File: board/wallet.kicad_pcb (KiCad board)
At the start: 4 copper layers, 48 x 85 mm, 108 parts, among them J1 TYPE-C-31-M-12, U1 BQ25185DLHR, U11 E73-2G4M08S1C, U12 ME6211C28M5G-N, U13 TPS60230RGTR, U14 TLV70313DBVR, U15 MAX17048G+T10, U2 TPS63802DLAR, U4 STM32U585VIT6Q, U5 SE050E2HQ1/Z01Z3Z, U6 TS3USB221ARSER, U7 SN74LVC1G02DBVR(UMW), U8 TPS22917DBVR, U9 TXU0202DCUR

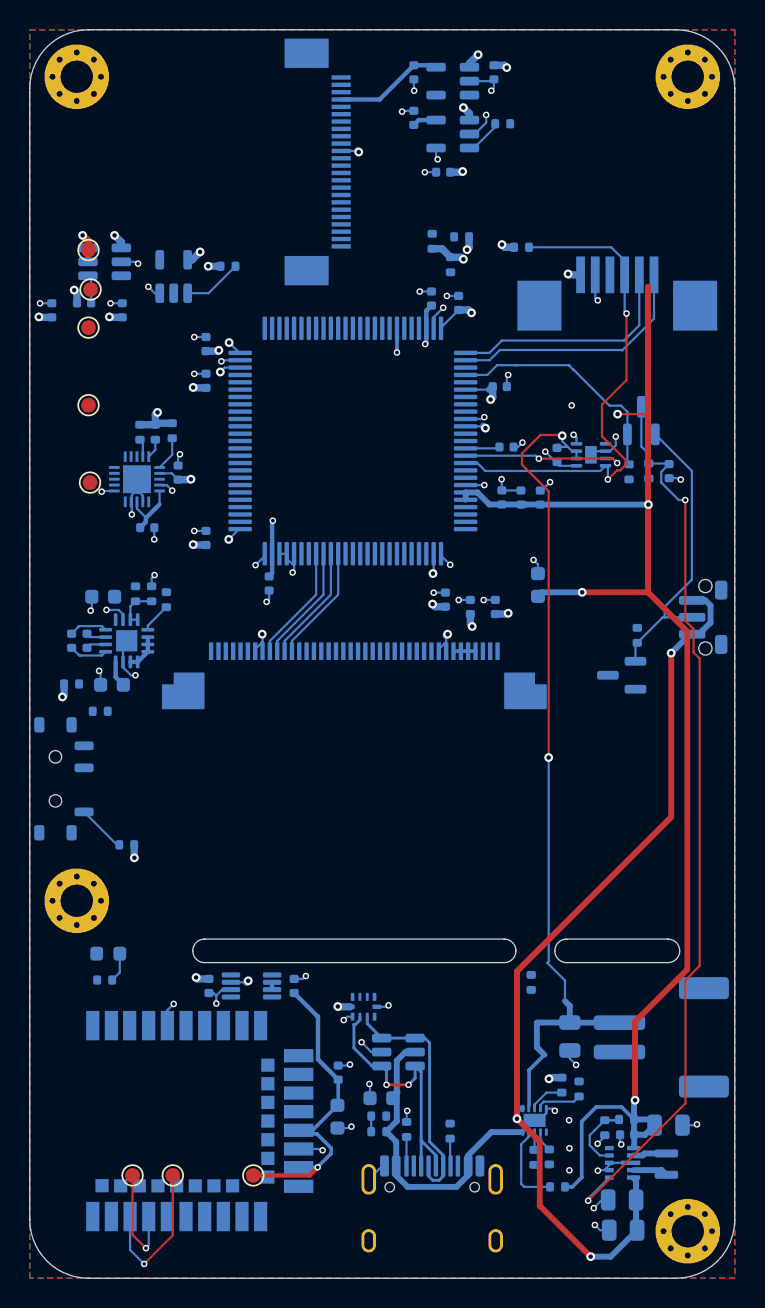
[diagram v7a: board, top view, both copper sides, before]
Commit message: Front copper freed: V3V3 runs made redundant by the In1 plane removed
With In1 a 3.3 V plane every V3V3 pin already has its via, so the owner's
3.3 V runs on the front copper carried nothing but took 64.6 mm of the layer
kept for the buses (incl. the 8.5 mm dangling stub). Removed with KiCad's own
unconnected count as the oracle: flat at 61 (the TP_3V3 front-pad link, which
did depend on it, is kept). The buck-boost's output now enters the plane
through three vias at C_3V3 (two added, each >= 0.25 mm of bare board from
every pad). Also: a 0.02 mm micro-jog on RADIO_3V3 (a 90-degree corner) gone.

Audit (carrier suite run on this board, its ledger and current budget are the
carrier's): of the craft/corner/snaking/width/return-path findings only the
RADIO_3V3 corner and a 2 mm FB_3V3 hop around a GND via were in my copper;
the rest are in the hand-routed chin and east side.

Co-Authored-By: Claude Opus 5.5 <noreply@anthropic.com>
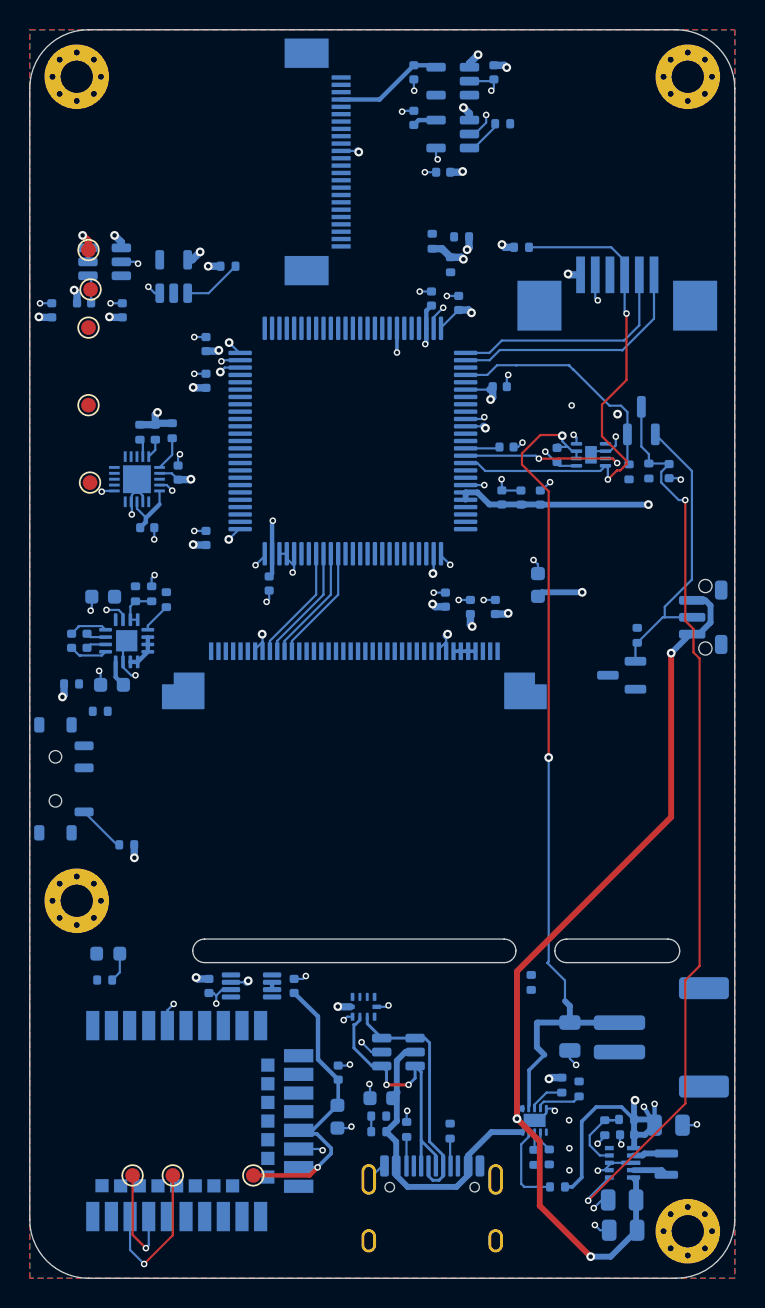
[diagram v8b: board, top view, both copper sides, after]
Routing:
- net V3V3: track 147.0 -> 85.3 mm, vias 43 -> 45
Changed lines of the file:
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@@
-	)
-	(segment
-		(start 42.09 26.01)
-		(end 42.09 17.49)
-		(width 0.4)
-		(layer "F.Cu")
-		(net "V3V3")
-	)
-	(segment
-		(start 42.09 38.3)
-		(end 42.09 26.01)
-		(width 0.4)
-		(layer "F.Cu")
-		(net "V3V3")
-	)
-	(segment
-		(start 37.61 38.3)
-		(end 42.09 38.3)
-		(width 0.4)
-		(layer "F.Cu")
-		(net "V3V3")
-	)
-	(segment
-		(start 44.76459 63.97541)
-		(end 41.21 67.53)
-		(width 0.4)
-		(layer "F.Cu")
-		(net "V3V3")
-	)
-	(segment
-		(start 42.09 38.3)
-		(end 44.76459 40.97459)
-		(width 0.4)
-		(layer "F.Cu")
-		(net "V3V3")
-	)
-	(segment
-		(start 44.76459 40.97459)
-		(end 44.76459 63.97541)
-		(width 0.4)
-		(layer "F.Cu")
-		(net "V3V3")
 	)
 	(segment
@@
 		(net "V3V3")
 	)
-	(segment
-		(start 40.02 26.17)
-		(end 41.93 26.17)
-		(width 0.15)
-		(layer "F.Cu")
-		(net "V3V3")
-	)
-	(segment
-		(start 41.93 26.17)
-		(end 42.09 26.01)
-		(width 0.15)
-		(layer "F.Cu")
-		(net "V3V3")
-	)
-	(segment
-		(start 41.21 67.53)
-		(end 41.21 72.88)
-		(width 0.4)
-		(layer "F.Cu")
-		(net "V3V3")
-	)
 	(via
 		(at 14.875 64.75)
@@
 	)
 	(via
+		(at 42.54 73.13)
+		(size 0.45)
+		(drill 0.25)
+		(layers "F.Cu" "B.Cu")
+		(net "V3V3")
+	)
+	(via
 		(at 10.975 30.6)
 		(size 0.6)
@@
 		(size 0.6)
 		(drill 0.3)
+		(layers "F.Cu" "B.Cu")
+		(net "V3V3")
+	)
+	(via
+		(at 41.815 73.324264)
+		(size 0.45)
+		(drill 0.25)
 		(layers "F.Cu" "B.Cu")
 		(net "V3V3")
@@
 	)
 	(segment
+		(start 42.54 74.58)
+		(end 42.54 73.13)
+		(width 0.3)
+		(layer "B.Cu")
+		(net "V3V3")
+	)
+	(segment
 		(start 20.995 66.52)
 		(end 20.975 66.5)
@@
 		(end 42.15 74.19)
 		(width 0.4)
+		(layer "B.Cu")
+		(net "V3V3")
+	)
+	(segment
+		(start 42.54 74.58)
+		(end 41.815 73.324264)
+		(width 0.3)
 		(layer "B.Cu")
 		(net "V3V3")
@@
 	)
 	(segment
-		(start 19.625 67.175)
-		(end 19.595001 67.175)
-		(width 0.3)
-		(layer "B.Cu")
-		(net "RADIO_3V3")
-	)
-	(segment
 		(start 19.24 75.13)
 		(end 19.24 74.935633)
@@
 	)
 	(segment
-		(start 19.595001 67.175)
+		(start 19.625 67.175)
 		(end 18 65.579999)
 		(width 0.3)
